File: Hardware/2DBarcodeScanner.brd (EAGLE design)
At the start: 44.5 x 22.9 mm, 58 parts, among them Q1 600mA/40V, Q2 600mA/40V, U1 3.3V

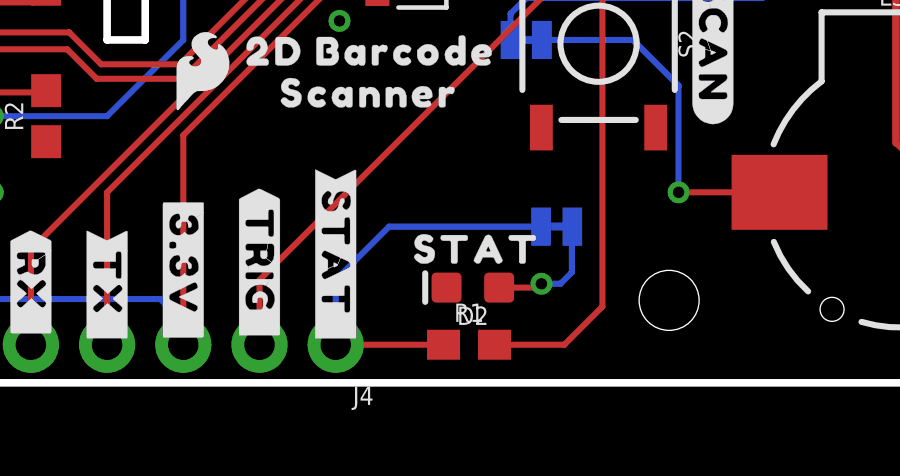
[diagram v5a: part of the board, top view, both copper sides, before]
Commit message: Change out green stat LED for yellow
Pull-up resistor 470 --> 1k ohm
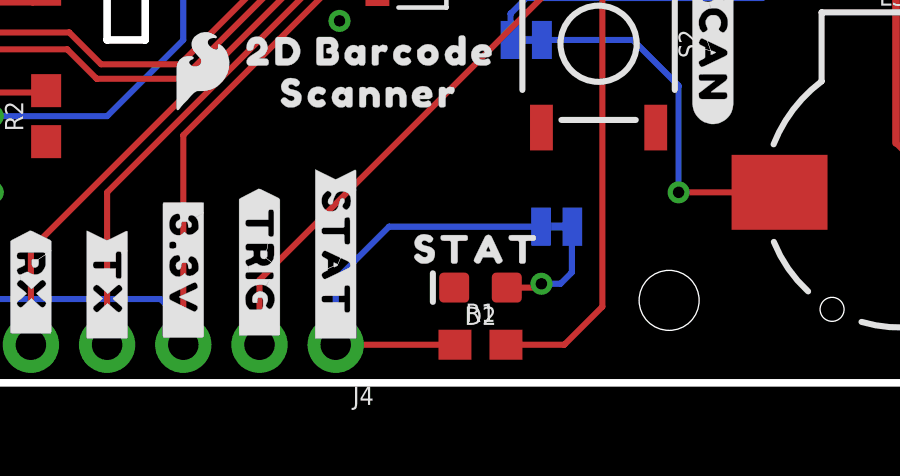
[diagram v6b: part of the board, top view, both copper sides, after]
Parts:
- D2: value GREEN -> Yellow
- R1: value 470 -> 1k
- moved R1 0.38 mm to (23.9, 1.27)
- moved D2 0.25 mm to (23.9, 3.17)
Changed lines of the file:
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@@
 <attribute name="VALUE" x="30.48" y="17.399" size="0.6096" layer="27" font="vector" ratio="20" align="top-center"/>
-</element>
-<element name="D2" library="SparkFun-LED" package="LED-0603" value="GREEN" x="23.622" y="3.175" smashed="yes" rot="R180">
-<attribute name="NAME" x="23.622" y="2.54" size="0.6096" layer="25" font="vector" ratio="20" rot="R180" align="bottom-center"/>
-<attribute name="PROD_ID" value="DIO-00821" x="23.622" y="3.175" size="1.778" layer="27" font="vector" ratio="15" rot="R180" display="off"/>
-<attribute name="VALUE" x="23.622" y="3.81" size="0.6096" layer="27" font="vector" ratio="20" rot="R180" align="top-center"/>
 </element>
 <element name="C3" library="SparkFun-Capacitors" package="0603" value="0.1uF" x="25.019" y="20.574" smashed="yes" rot="R180">
@@
 <attribute name="DESIGNER" value="Nobody" x="0" y="0" size="1.778" layer="27" font="vector" ratio="15" display="off"/>
 <attribute name="VERSION" value="v01" x="0" y="0" size="1.778" layer="27" font="vector" ratio="15" display="off"/>
-</element>
-<element name="R1" library="SparkFun-Resistors" package="0603" value="470" x="23.495" y="1.27" smashed="yes">
-<attribute name="NAME" x="23.495" y="2.032" size="0.6096" layer="25" font="vector" ratio="20" align="bottom-center"/>
-<attribute name="PROD_ID" value="RES-07869" x="23.495" y="1.27" size="1.778" layer="27" font="vector" ratio="15" display="off"/>
-<attribute name="VALUE" x="23.495" y="0.508" size="0.6096" layer="27" font="vector" ratio="20" align="top-center"/>
 </element>
 <element name="J4" library="SparkFun-Connectors" package="1X06_NO_SILK" value="" x="19.05" y="1.27" smashed="yes" rot="R180">
@@
 <element name="U$6" library="output" package="#STAT#0" value="" x="25.654" y="5.207" smashed="yes" rot="MR0"/>
 <element name="U$7" library="output" package="#3#3V#0" value="" x="7.62" y="18.288" smashed="yes" rot="MR270"/>
+<element name="D2" library="SparkFun-LED" package="LED-0603" value="Yellow" x="23.876" y="3.175" smashed="yes" rot="R180">
+<attribute name="NAME" x="23.876" y="2.54" size="0.6096" layer="25" font="vector" ratio="20" rot="R180" align="bottom-center"/>
+<attribute name="PROD_ID" value="DIO-09003" x="23.876" y="3.175" size="1.778" layer="27" font="vector" ratio="15" rot="R180" display="off"/>
+<attribute name="VALUE" x="23.876" y="3.81" size="0.6096" layer="27" font="vector" ratio="20" rot="R180" align="top-center"/>
+</element>
+<element name="R1" library="SparkFun-Resistors" package="0603" value="1k" x="23.876" y="1.27" smashed="yes">
+<attribute name="NAME" x="23.876" y="2.032" size="0.6096" layer="25" font="vector" ratio="20" align="bottom-center"/>
+<attribute name="PROD_ID" value="RES-07856" x="23.876" y="1.27" size="1.778" layer="27" font="vector" ratio="15" display="off"/>
+<attribute name="VALUE" x="23.876" y="0.508" size="0.6096" layer="27" font="vector" ratio="20" align="top-center"/>
+</element>
 </elements>
 <signals>
@@
 <contactref element="R8" pad="1"/>
 <contactref element="Q1" pad="2"/>
-<contactref element="D2" pad="C"/>
 <contactref element="R10" pad="1"/>
 <contactref element="C3" pad="2"/>
@@
 <contactref element="J3" pad="10"/>
 <via x="7.62" y="6.35" extent="1-16" drill="0.381"/>
+<contactref element="D2" pad="C"/>
 </signal>
 <signal name="3.3V" class="1">
@@
 <signal name="N$4">
 <contactref element="Q2" pad="2"/>
-<contactref element="R1" pad="2"/>
 <wire x1="29.48" y1="18.1" x2="29.439" y2="18.059" width="0.2032" layer="1"/>
 <wire x1="29.439" y1="16.739" x2="29.439" y2="18.059" width="0.2032" layer="1"/>
 <wire x1="27.94" y1="15.24" x2="29.439" y2="16.739" width="0.2032" layer="1"/>
-<wire x1="24.345" y1="1.27" x2="26.67" y2="1.27" width="0.2032" layer="1"/>
 <wire x1="26.67" y1="1.27" x2="27.94" y2="2.54" width="0.2032" layer="1"/>
 <wire x1="27.94" y1="2.54" x2="27.94" y2="15.24" width="0.2032" layer="1"/>
+<contactref element="R1" pad="2"/>
+<wire x1="24.726" y1="1.27" x2="26.67" y2="1.27" width="0.2032" layer="1"/>
 </signal>
 <signal name="N$7">
@@
 </signal>
 <signal name="STATUS_OUT">
-<contactref element="R1" pad="1"/>
 <contactref element="JP1" pad="2"/>
 <contactref element="J4" pad="1"/>
@@
 <wire x1="20.828" y1="5.207" x2="19.05" y2="3.429" width="0.2032" layer="16"/>
 <wire x1="19.05" y1="1.27" x2="19.05" y2="3.429" width="0.2032" layer="16"/>
-<wire x1="22.645" y1="1.27" x2="19.05" y2="1.27" width="0.2032" layer="1"/>
+<contactref element="R1" pad="1"/>
+<wire x1="23.026" y1="1.27" x2="19.05" y2="1.27" width="0.2032" layer="1"/>
 </signal>
 <signal name="N$8">
 <contactref element="JP1" pad="1"/>
-<contactref element="D2" pad="A"/>
 <wire x1="26.9367" y1="5.207" x2="26.924" y2="5.1943" width="0.2032" layer="16"/>
 <wire x1="26.924" y1="5.1943" x2="26.924" y2="3.683" width="0.2032" layer="16"/>
@@
 <wire x1="26.543" y1="3.302" x2="25.908" y2="3.302" width="0.2032" layer="16"/>
 <wire x1="25.781" y1="3.175" x2="25.908" y2="3.302" width="0.2032" layer="1"/>
-<wire x1="25.781" y1="3.175" x2="24.499" y2="3.175" width="0.2032" layer="1"/>
 <via x="25.908" y="3.302" extent="1-16" drill="0.381"/>
+<contactref element="D2" pad="A"/>
+<wire x1="24.753" y1="3.175" x2="25.781" y2="3.175" width="0.2032" layer="1"/>
 </signal>
 <signal name="N$1">

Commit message: Switch yellow stat LED out for blue
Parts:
- D2: value Yellow -> BLUE
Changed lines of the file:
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@@
 <attribute name="VALUE" x="2.54" y="11.43" size="0.762" layer="27" rot="R270" align="center"/>
 </element>
-<element name="U$1" library="SparkFun-Hardware" package="BARCODE_SCANNER_MOUNT" value="BARCODE_SCANNER_MOUNT" x="35.814" y="11.049" smashed="yes" rot="MR180"/>
+<element name="U$1" library="SparkFun-Hardware" package="BARCODE_SCANNER_MOUNT" value="BARCODE_SCANNER_MOUNT" x="35.814" y="11.049" smashed="yes" rot="MR180">
+<attribute name="PROD_ID" value="LPA-14926" x="35.814" y="11.049" size="1.778" layer="28" rot="MR180" display="off"/>
+</element>
 <element name="U1" library="SparkFun-IC-Power" package="SOT23-5" value="3.3V" x="15.24" y="17.907" smashed="yes" rot="R180">
 <attribute name="NAME" x="16.129" y="15.748" size="0.4064" layer="25" rot="R180"/>
@@
 <element name="U$6" library="output" package="#STAT#0" value="" x="25.654" y="5.207" smashed="yes" rot="MR0"/>
 <element name="U$7" library="output" package="#3#3V#0" value="" x="7.62" y="18.288" smashed="yes" rot="MR270"/>
-<element name="D2" library="SparkFun-LED" package="LED-0603" value="Yellow" x="23.876" y="3.175" smashed="yes" rot="R180">
-<attribute name="NAME" x="23.876" y="2.54" size="0.6096" layer="25" font="vector" ratio="20" rot="R180" align="bottom-center"/>
-<attribute name="PROD_ID" value="DIO-09003" x="23.876" y="3.175" size="1.778" layer="27" font="vector" ratio="15" rot="R180" display="off"/>
-<attribute name="VALUE" x="23.876" y="3.81" size="0.6096" layer="27" font="vector" ratio="20" rot="R180" align="top-center"/>
-</element>
 <element name="R1" library="SparkFun-Resistors" package="0603" value="1k" x="23.876" y="1.27" smashed="yes">
 <attribute name="NAME" x="23.876" y="2.032" size="0.6096" layer="25" font="vector" ratio="20" align="bottom-center"/>
@@
 <attribute name="VALUE" x="23.876" y="0.508" size="0.6096" layer="27" font="vector" ratio="20" align="top-center"/>
 </element>
+<element name="D2" library="SparkFun-LED" package="LED-0603" value="BLUE" x="23.876" y="3.175" smashed="yes" rot="R180">
+<attribute name="NAME" x="23.876" y="2.54" size="0.6096" layer="25" font="vector" ratio="20" rot="R180" align="bottom-center"/>
+<attribute name="PROD_ID" value="DIO-08575" x="23.876" y="3.175" size="1.778" layer="27" font="vector" ratio="15" rot="R180" display="off"/>
+<attribute name="VALUE" x="23.876" y="3.81" size="0.6096" layer="27" font="vector" ratio="20" rot="R180" align="top-center"/>
+</element>
 </elements>

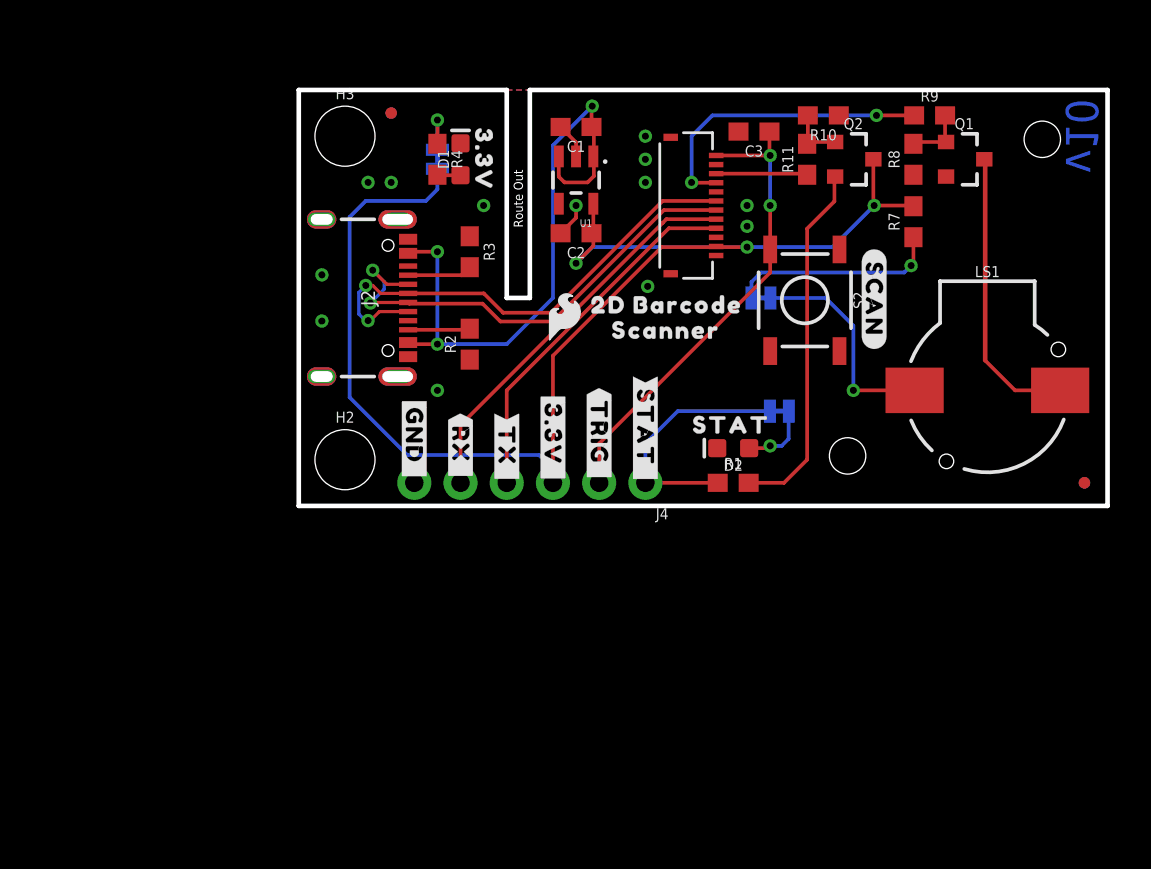
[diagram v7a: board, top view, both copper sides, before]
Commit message: Design Review Changes
Update schematic frame
Dimension width 0.008
Increased width of GND polygon
Moved v10 label on bottom
Moved bottom jumpers in-line
Added measures
Made y-axis of board 1-in, mounting holes on 0.8in
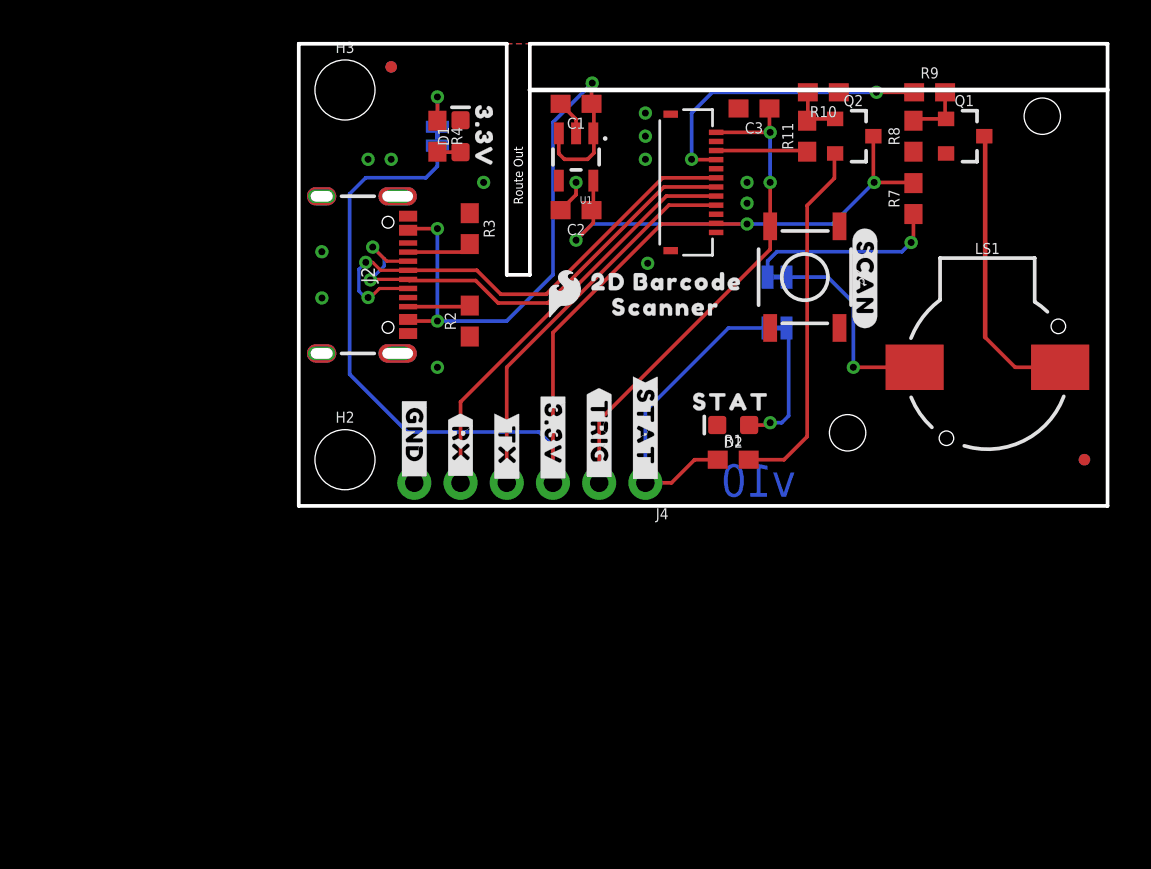
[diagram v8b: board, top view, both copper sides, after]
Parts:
- FRAME1: value FRAME-LETTERNO_PACKAGE -> FRAME-LETTER; device SparkFun-Aesthetics:DUMMY -> SparkFun-Aesthetics:CREATIVE_COMMONS
- moved FRAME1 10.2 mm to (1.27, -10.2)
- moved U$6 4.58 mm to (25.4, 9.78)
- moved JP1 4.57 mm to (26.3, 9.78)
- moved FD1 2.54 mm to (5.08, 24.1)
- moved FD4 2.54 mm to (5.08, 24.1)
- moved H3 2.54 mm to (2.54, 22.9)
- moved LOGO3 2.54 mm to (20.3, 23.4)
- moved BUZZ 1.45 mm to (26.3, 12.6)
- moved U$5 1.45 mm to (25.4, 12.6)
- moved U$20 1.27 mm to (27.4, 18.5)
- moved U$1 1.27 mm to (35.8, 12.3)
- moved U$17 1.27 mm to (15.4, 12.3)
- moved U$19 1.27 mm to (16.5, 10.9)
- moved D2 1.27 mm to (23.9, 4.45)
- moved LS1 1.27 mm to (37.8, 7.62)
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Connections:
- net SCAN_TRIGGER renamed !SCAN_TRIGGER!
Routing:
- net N$8: track 3.91 -> 7.25 mm
- net STATUS_OUT: track 13.7 -> 17.1 mm
- net 3.3V: track 76.5 -> 79.1 mm
- net TXO: track 20.3 -> 21.6 mm
- net RXI: track 21.9 -> 23.2 mm
- net !SCAN_TRIGGER!: track 26.2 -> 27.5 mm
- net N$3: track 12.1 -> 11.2 mm
- net N$1: track 11.6 -> 10.8 mm
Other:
- board size 44.5 x 22.9 mm -> 44.5 x 25.4 mm
- board text added: "Nick Poole Revised by: Priyanka Makin"
- board text removed: "Original Design by: Nick Poole Revised by: Priyanka Makin"
